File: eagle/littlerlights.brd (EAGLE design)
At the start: 15.2 x 8.9 mm, 8 parts, among them U1 Tiny85-20-SMT

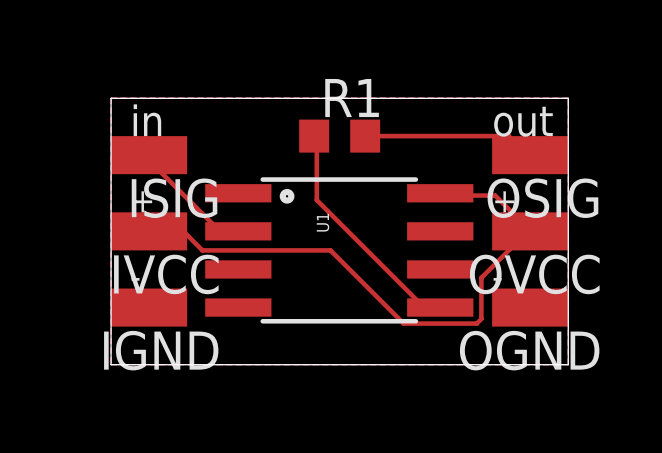
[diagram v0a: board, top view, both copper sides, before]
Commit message: Make the little lights actually little
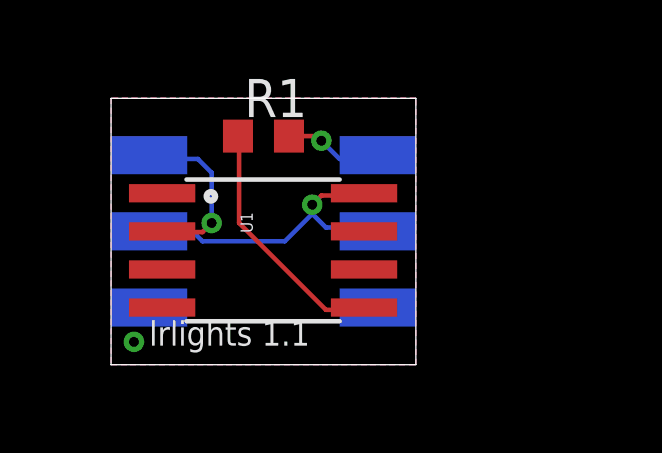
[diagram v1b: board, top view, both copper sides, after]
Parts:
- moved OGND 5.08 mm to (8.89, 1.91), flipped to the bottom
- moved OSIG 5.08 mm to (8.89, 6.99), flipped to the bottom
- moved OVCC 5.08 mm to (8.89, 4.45), flipped to the bottom
- moved R1 2.54 mm to (5.08, 7.62)
- moved U1 2.54 mm to (5.08, 3.81)
- flipped IGND to the bottom
- flipped ISIG to the bottom
- flipped IVCC to the bottom
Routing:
- net VCC: track 19.6 -> 10.6 mm, vias 0 -> 1
- net ~: track 5.76 -> 3.36 mm, vias 0 -> 1
- net OUT: track 4.16 -> 5.79 mm, vias 0 -> 1
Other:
- board size 15.2 x 8.9 mm -> 10.2 x 8.9 mm
- board text added: "lrlights 1.1"
- board text removed: "littlerlights 1.0"
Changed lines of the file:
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@@
 <board>
 <plain>
-<wire x1="0" y1="0" x2="15.24" y2="0" width="0" layer="20"/>
-<wire x1="15.24" y1="0" x2="15.24" y2="8.88" width="0" layer="20"/>
-<wire x1="15.24" y1="8.88" x2="0" y2="8.88" width="0" layer="20"/>
+<wire x1="0" y1="0" x2="10.16" y2="0" width="0" layer="20"/>
+<wire x1="10.16" y1="0" x2="10.16" y2="8.88" width="0" layer="20"/>
+<wire x1="10.16" y1="8.88" x2="0" y2="8.88" width="0" layer="20"/>
 <wire x1="0" y1="8.88" x2="0" y2="0" width="0" layer="20"/>
-<text x="0.635" y="7.62" size="1.016" layer="21" font="vector">in</text>
-<text x="12.7" y="7.62" size="1.016" layer="21" font="vector">out</text>
-<text x="13.97" y="3.81" size="0.8128" layer="22" font="fixed" rot="MR0">littlerlights 1.0</text>
-<text x="0.635" y="2.54" size="0.8128" layer="21">-</text>
-<text x="12.7" y="2.54" size="0.8128" layer="21">-</text>
-<text x="12.7" y="5.08" size="0.8128" layer="21">+</text>
-<text x="0.635" y="5.08" size="0.8128" layer="21">+</text>
+<text x="1.905" y="7.62" size="1.016" layer="22" font="vector" rot="MR0">in</text>
+<text x="10.16" y="7.62" size="1.016" layer="22" font="vector" rot="MR0">out</text>
+<text x="1.27" y="0.635" size="0.8128" layer="21" font="fixed">lrlights 1.1</text>
+<text x="0.635" y="2.54" size="0.8128" layer="22" rot="MR0">-</text>
+<text x="10.16" y="2.54" size="0.8128" layer="22" rot="MR0">-</text>
+<text x="10.16" y="5.08" size="0.8128" layer="22" rot="MR0">+</text>
+<text x="1.905" y="5.08" size="0.8128" layer="22" rot="MR0">+</text>
 </plain>
 <attributes>
@@
 <param name="RoutingGrid" value="12.5mil"/>
 <param name="AutoGrid" value="1"/>
-<param name="Efforts" value="0"/>
+<param name="Efforts" value="2"/>
 <param name="TopRouterVariant" value="1"/>
 <param name="tpViaShape" value="round"/>
@@
 </autorouter>
 <elements>
-<element name="R1" library="resistor" package="R0603" value="470" x="7.62" y="7.62">
-<attribute name="DIGIKEY" value="MCT0603-470-CFCT-ND" x="7.62" y="7.62" size="1.778" layer="27" display="off"/>
+<element name="R1" library="resistor" package="R0603" value="470" x="5.08" y="7.62">
+<attribute name="DIGIKEY" value="MCT0603-470-CFCT-ND" x="5.08" y="7.62" size="1.778" layer="27" display="off"/>
 </element>
-<element name="U1" library="SparkFun-DigitalIC" package="SO08-EIAJ" value="Tiny85-20-SMT" x="7.62" y="3.81" rot="R270">
-<attribute name="PROD_ID" value="IC-09092" x="7.62" y="3.81" size="1.778" layer="27" rot="R270" display="off"/>
-<attribute name="DIGIKEY" value="ATTINY85-20SHRCT-ND" x="7.62" y="3.81" size="1.778" layer="27" rot="R270" display="off"/>
+<element name="U1" library="SparkFun-DigitalIC" package="SO08-EIAJ" value="Tiny85-20-SMT" x="5.08" y="3.81" rot="R270">
+<attribute name="PROD_ID" value="IC-09092" x="5.08" y="3.81" size="1.778" layer="27" rot="R270" display="off"/>
+<attribute name="DIGIKEY" value="ATTINY85-20SHRCT-ND" x="5.08" y="3.81" size="1.778" layer="27" rot="R270" display="off"/>
 </element>
-<element name="OSIG" library="wirepad" package="SMD1,27-2,54" value="" x="13.97" y="6.985" rot="R90"/>
-<element name="OVCC" library="wirepad" package="SMD1,27-2,54" value="" x="13.97" y="4.445" rot="R90"/>
-<element name="OGND" library="wirepad" package="SMD1,27-2,54" value="" x="13.97" y="1.905" rot="R90"/>
-<element name="ISIG" library="wirepad" package="SMD1,27-2,54" value="" x="1.27" y="6.985" rot="R90"/>
-<element name="IVCC" library="wirepad" package="SMD1,27-2,54" value="" x="1.27" y="4.445" rot="R90"/>
-<element name="IGND" library="wirepad" package="SMD1,27-2,54" value="" x="1.27" y="1.905" rot="R90"/>
+<element name="OSIG" library="wirepad" package="SMD1,27-2,54" value="" x="8.89" y="6.985" rot="MR90"/>
+<element name="OVCC" library="wirepad" package="SMD1,27-2,54" value="" x="8.89" y="4.445" rot="MR90"/>
+<element name="OGND" library="wirepad" package="SMD1,27-2,54" value="" x="8.89" y="1.905" rot="MR90"/>
+<element name="ISIG" library="wirepad" package="SMD1,27-2,54" value="" x="1.27" y="6.985" rot="MR90"/>
+<element name="IVCC" library="wirepad" package="SMD1,27-2,54" value="" x="1.27" y="4.445" rot="MR90"/>
+<element name="IGND" library="wirepad" package="SMD1,27-2,54" value="" x="1.27" y="1.905" rot="MR90"/>
 </elements>
 <signals>
@@
 <contactref element="IVCC" pad="1"/>
 <contactref element="OVCC" pad="1"/>
-<wire x1="12.8016" y1="5.6388" x2="10.9728" y2="5.6388" width="0.1524" layer="1"/>
-<wire x1="13.8684" y1="4.572" x2="12.8016" y2="5.6388" width="0.1524" layer="1"/>
-<wire x1="10.9728" y1="5.6388" x2="10.9728" y2="5.715" width="0.1524" layer="1"/>
-<wire x1="13.8684" y1="4.572" x2="13.97" y2="4.445" width="0.1524" layer="1"/>
-<wire x1="2.4384" y1="4.4196" x2="1.3716" y2="4.4196" width="0.1524" layer="1"/>
-<wire x1="3.048" y1="3.81" x2="2.4384" y2="4.4196" width="0.1524" layer="1"/>
-<wire x1="7.3152" y1="3.81" x2="3.048" y2="3.81" width="0.1524" layer="1"/>
-<wire x1="9.7536" y1="1.3716" x2="7.3152" y2="3.81" width="0.1524" layer="1"/>
-<wire x1="12.192" y1="1.3716" x2="9.7536" y2="1.3716" width="0.1524" layer="1"/>
-<wire x1="12.3444" y1="1.524" x2="12.192" y2="1.3716" width="0.1524" layer="1"/>
-<wire x1="12.3444" y1="2.8956" x2="12.3444" y2="1.524" width="0.1524" layer="1"/>
-<wire x1="13.8684" y1="4.4196" x2="12.3444" y2="2.8956" width="0.1524" layer="1"/>
-<wire x1="1.3716" y1="4.4196" x2="1.27" y2="4.445" width="0.1524" layer="1"/>
-<wire x1="13.8684" y1="4.4196" x2="13.97" y2="4.445" width="0.1524" layer="1"/>
+<wire x1="7.0104" y1="5.6388" x2="8.382" y2="5.6388" width="0.1524" layer="1"/>
+<wire x1="6.7056" y1="5.334" x2="7.0104" y2="5.6388" width="0.1524" layer="1"/>
+<wire x1="7.1628" y1="4.572" x2="6.7056" y2="5.0292" width="0.1524" layer="16"/>
+<wire x1="8.8392" y1="4.572" x2="7.1628" y2="4.572" width="0.1524" layer="16"/>
+<wire x1="8.382" y1="5.6388" x2="8.4328" y2="5.715" width="0.1524" layer="1"/>
+<wire x1="8.8392" y1="4.572" x2="8.89" y2="4.445" width="0.1524" layer="16"/>
+<wire x1="2.7432" y1="4.4196" x2="1.3716" y2="4.4196" width="0.1524" layer="16"/>
+<wire x1="3.048" y1="4.1148" x2="2.7432" y2="4.4196" width="0.1524" layer="16"/>
+<wire x1="5.7912" y1="4.1148" x2="3.048" y2="4.1148" width="0.1524" layer="16"/>
+<wire x1="6.7056" y1="5.0292" x2="5.7912" y2="4.1148" width="0.1524" layer="16"/>
+<wire x1="1.3716" y1="4.4196" x2="1.27" y2="4.445" width="0.1524" layer="16"/>
+<wire x1="6.7056" y1="5.0292" x2="6.7056" y2="5.334" width="0.1524" layer="16"/>
+<via x="6.7056" y="5.334" extent="1-16" drill="0.3302"/>
 </signal>
 <signal name="MOSI">
 <contactref element="U1" pad="5"/>
 <contactref element="R1" pad="1"/>
-<wire x1="6.858" y1="5.4864" x2="6.858" y2="7.62" width="0.1524" layer="1"/>
-<wire x1="10.3632" y1="1.9812" x2="6.858" y2="5.4864" width="0.1524" layer="1"/>
-<wire x1="10.9728" y1="1.9812" x2="10.3632" y2="1.9812" width="0.1524" layer="1"/>
-<wire x1="6.858" y1="7.62" x2="6.77" y2="7.62" width="0.1524" layer="1"/>
-<wire x1="10.9728" y1="1.9812" x2="10.9728" y2="1.905" width="0.1524" layer="1"/>
+<wire x1="4.2672" y1="4.7244" x2="4.2672" y2="7.62" width="0.1524" layer="1"/>
+<wire x1="7.1628" y1="1.8288" x2="4.2672" y2="4.7244" width="0.1524" layer="1"/>
+<wire x1="8.382" y1="1.8288" x2="7.1628" y2="1.8288" width="0.1524" layer="1"/>
+<wire x1="4.2672" y1="7.62" x2="4.23" y2="7.62" width="0.1524" layer="1"/>
+<wire x1="8.382" y1="1.8288" x2="8.4328" y2="1.905" width="0.1524" layer="1"/>
 </signal>
 <signal name="GND">
@@
 <polygon width="0.4064" layer="16">
 <vertex x="0" y="0"/>
-<vertex x="15.24" y="0"/>
-<vertex x="15.24" y="8.89"/>
+<vertex x="10.16" y="0"/>
+<vertex x="10.16" y="8.89"/>
 <vertex x="0" y="8.89"/>
 </polygon>
@@
 <vertex x="0" y="8.89"/>
 <vertex x="0" y="0"/>
-<vertex x="15.24" y="0"/>
-<vertex x="15.24" y="8.89"/>
+<vertex x="10.16" y="0"/>
+<vertex x="10.16" y="8.89"/>
 </polygon>
 <contactref element="IGND" pad="1"/>
 <contactref element="OGND" pad="1"/>
+<via x="0.762" y="0.762" extent="1-16" drill="0.3302"/>
 </signal>
 <signal name="OUT">
 <contactref element="U1" pad="2"/>
 <contactref element="ISIG" pad="1"/>
-<wire x1="3.5052" y1="4.572" x2="4.1148" y2="4.572" width="0.1524" layer="1"/>
-<wire x1="1.2192" y1="6.858" x2="3.5052" y2="4.572" width="0.1524" layer="1"/>
-<wire x1="4.1148" y1="4.572" x2="4.2418" y2="4.445" width="0.1524" layer="1"/>
-<wire x1="1.2192" y1="6.858" x2="1.27" y2="6.985" width="0.1524" layer="1"/>
+<wire x1="3.048" y1="4.4196" x2="1.8288" y2="4.4196" width="0.1524" layer="1"/>
+<wire x1="3.3528" y1="4.7244" x2="3.048" y2="4.4196" width="0.1524" layer="1"/>
+<wire x1="3.3528" y1="6.4008" x2="3.3528" y2="4.7244" width="0.1524" layer="16"/>
+<wire x1="2.8956" y1="6.858" x2="3.3528" y2="6.4008" width="0.1524" layer="16"/>
+<wire x1="1.3716" y1="6.858" x2="2.8956" y2="6.858" width="0.1524" layer="16"/>
+<wire x1="1.8288" y1="4.4196" x2="1.7018" y2="4.445" width="0.1524" layer="1"/>
+<wire x1="1.3716" y1="6.858" x2="1.27" y2="6.985" width="0.1524" layer="16"/>
+<via x="3.3528" y="4.7244" extent="1-16" drill="0.3302"/>
 </signal>
 <signal name="~">
 <contactref element="R1" pad="2"/>
 <contactref element="OSIG" pad="1"/>
-<wire x1="13.2588" y1="7.62" x2="8.47" y2="7.62" width="0.1524" layer="1"/>
-<wire x1="13.8684" y1="7.0104" x2="13.2588" y2="7.62" width="0.1524" layer="1"/>
-<wire x1="13.8684" y1="7.0104" x2="13.97" y2="6.985" width="0.1524" layer="1"/>
+<wire x1="6.858" y1="7.62" x2="5.93" y2="7.62" width="0.1524" layer="1"/>
+<wire x1="7.0104" y1="7.4676" x2="6.858" y2="7.62" width="0.1524" layer="1"/>
+<wire x1="7.62" y1="6.858" x2="7.0104" y2="7.4676" width="0.1524" layer="16"/>
+<wire x1="8.8392" y1="6.858" x2="7.62" y2="6.858" width="0.1524" layer="16"/>
+<wire x1="8.8392" y1="6.858" x2="8.89" y2="6.985" width="0.1524" layer="16"/>
+<via x="7.0104" y="7.4676" extent="1-16" drill="0.3302"/>
 </signal>
 </signals>
